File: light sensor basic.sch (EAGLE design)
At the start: 1 part

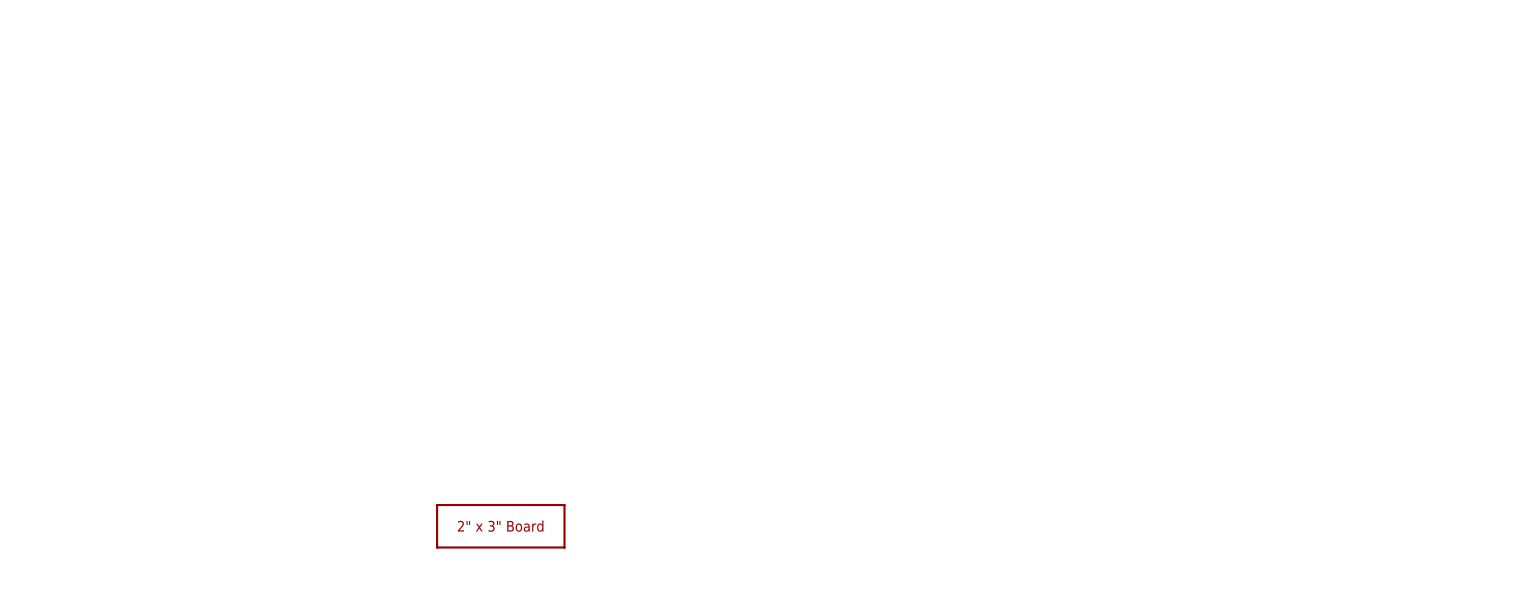
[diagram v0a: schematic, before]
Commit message: schematic drawn
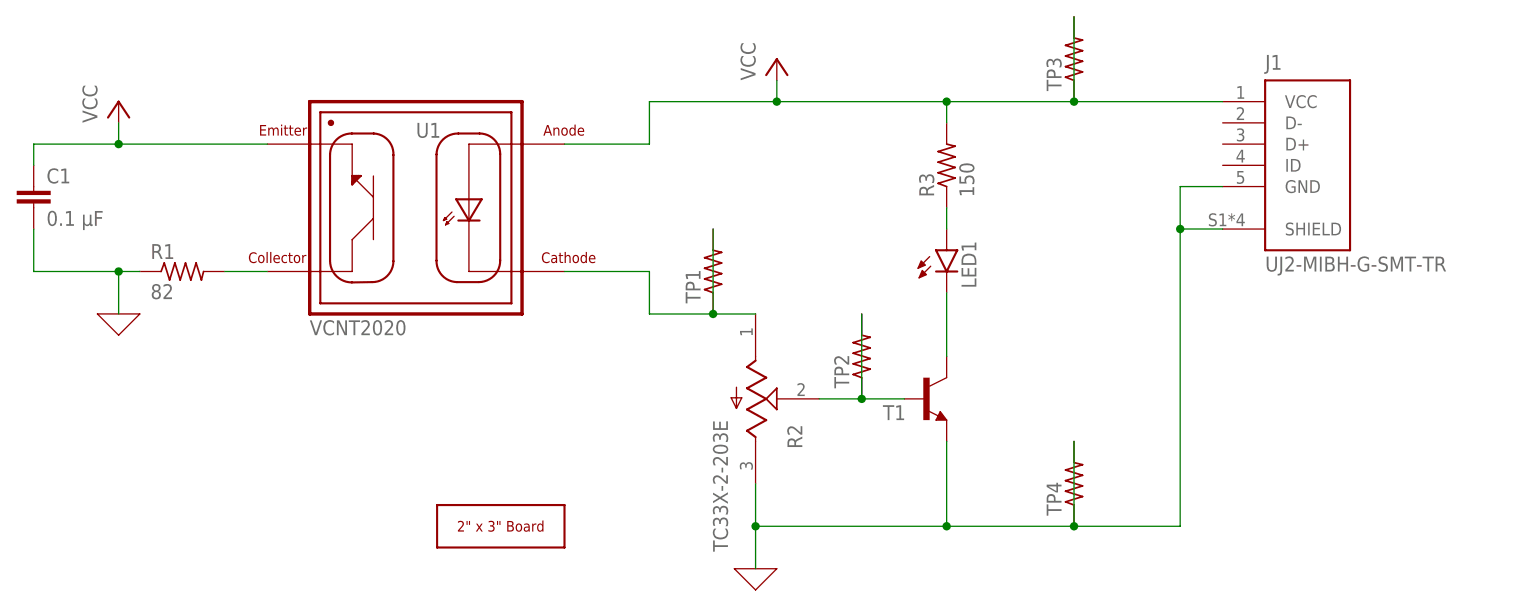
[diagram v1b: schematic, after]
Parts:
- added C1: 0.1 µF, rcl:C-EUC1206
- added J1: UJ2-MIBH-G-SMT-TR, UJ2-MIBH-G-SMT-TR:UJ2-MIBH-G-SMT-TR
- added LED1: (no value), led:LEDCHIPLED_0805
- added R1: 82, rcl:R-US_R0805
- added R2: TC33X-2-203E, TC33X-2-203E:TC33X-2-203E
- added R3: 150, rcl:R-US_R0805
- added T1: (no value), transistor:BFS17-NPN-SOT23-BEC
- added TP1, TP2, TP3, TP4: (no value), rcl:R-US_R1206
- added U1: VCNT2020, VCNT2020:VCNT2020
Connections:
- new net 0: C1.2, J1.GND, J1.SHIELD, R1.1, R2.CW, T1.E, TP4.1, TP4.2
- new net N$1: R2.W, T1.B, TP2.1, TP2.2
- new net N$2: R1.2, U1.COLLECTOR
- new net N$3: LED1.C, T1.C
- new net N$5: R2.CCW, TP1.1, TP1.2, U1.CATHODE
- new net N$8: LED1.A, R3.1
- new net VCC: C1.1, J1.VCC, R3.2, TP3.1, TP3.2, U1.ANODE, U1.EMITTER
